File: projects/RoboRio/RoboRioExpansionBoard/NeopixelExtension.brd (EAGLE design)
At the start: 34.2 x 12.7 mm, 6 parts, among them J1 POWER, P1 Input, U1 74AHCT1G08

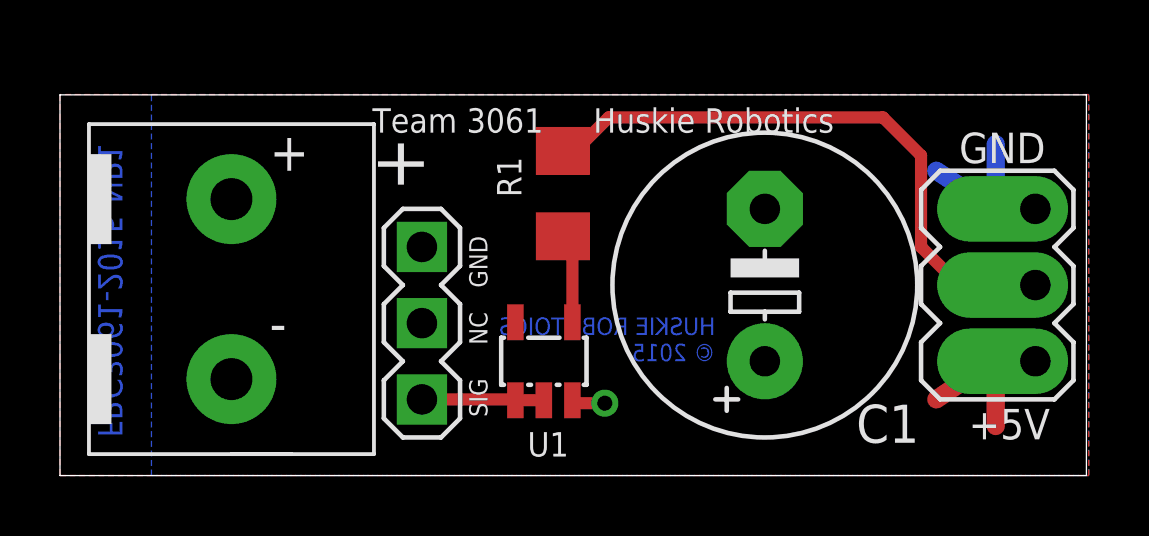
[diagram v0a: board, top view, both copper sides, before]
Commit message: Updated copyright signs to not use © symbol
since that symbol doesn't work with vector fonts.
Also regenerated all gerber files.
Put all gerbers into 2 zips to send to MPCS
We are done with the board!!!!
(I hope)
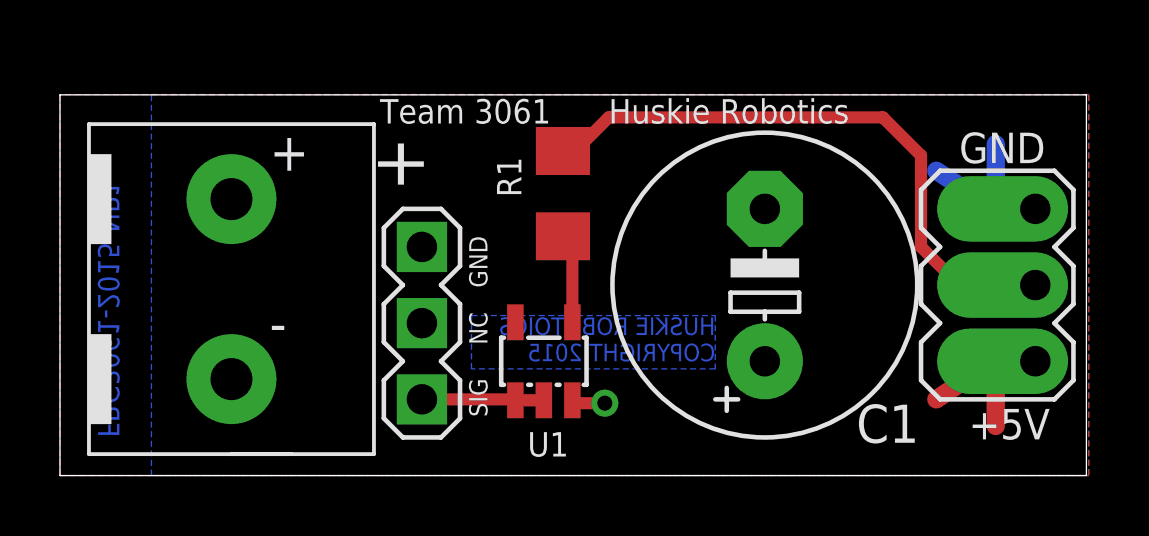
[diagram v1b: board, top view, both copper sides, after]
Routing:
- added copper zone on layer 16, net N$3
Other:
- board text added: "HUSKIE ROBOTOICS COPYRIGHT 2015"
- board text removed: "HUSKIE ROBOTOICS © 2015"
